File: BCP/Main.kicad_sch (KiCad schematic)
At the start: 7 parts, among them SW1 SW_Nidec_CAS-120A1, U1 LD1117V33, U2 Pico 2, U3 DEV-13712

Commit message: Removed autosave (I swear I know what I'm doing)
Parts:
- added D1, D2, D3, D4: LED, symbol Device:LED
- added Q1: PMOS, symbol Simulation_SPICE:PMOS
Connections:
- net 3.3 V: now also D1.2 (A)
- net GND: now also D2.1 (K), D3.1 (K), D4.1 (K), Q1.1 (D)
- net FLIGHTLED: now reaches U2.24 (GPIO18)
- net FLIGHTLED: now also Q1.2 (G)
- net DEBUG3: now reaches U2.25 (GPIO19)
- net DEBUG3: now also D4.2 (A)
- net DEBUG2: now reaches U2.26 (GPIO20)
- net DEBUG2: now also D3.2 (A)
- net DEBUG1: now reaches U2.27 (GPIO21)
- net DEBUG1: now also D2.2 (A)
- new net: D1.1 (K), Q1.3 (S)
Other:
- note added: "LEDs"
- moved on the sheet: U2

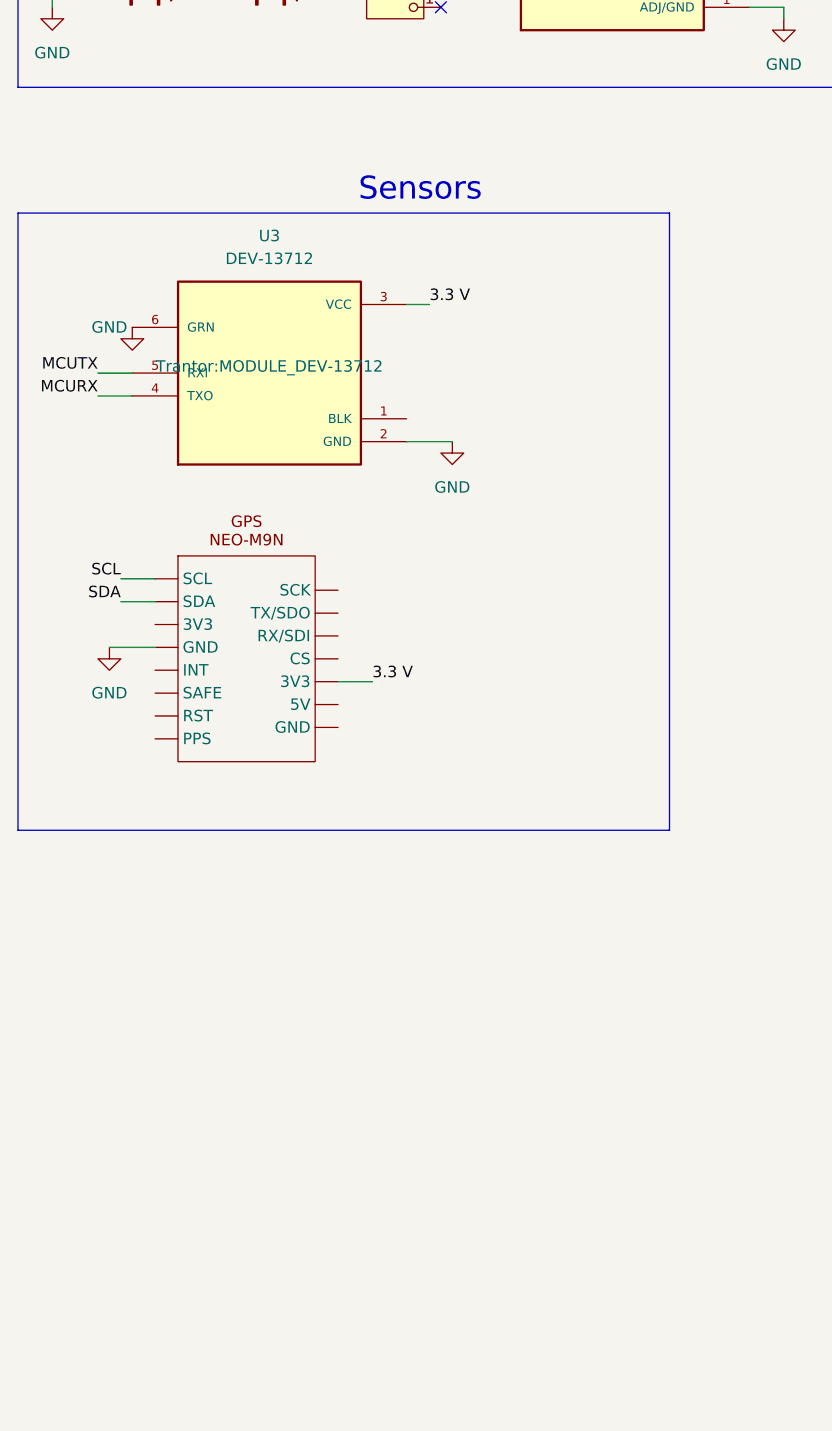
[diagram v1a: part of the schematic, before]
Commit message: Added GPS and BME
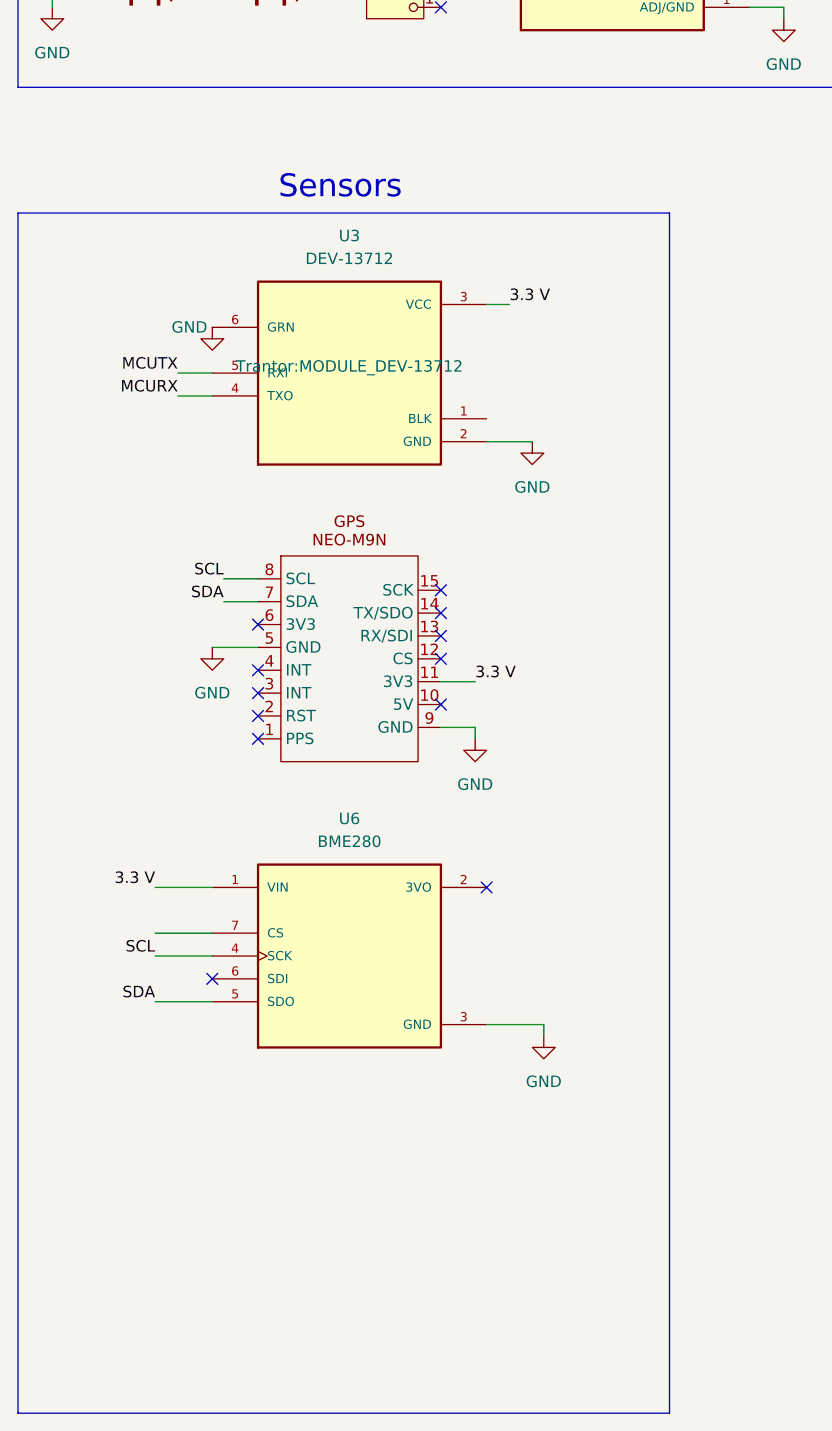
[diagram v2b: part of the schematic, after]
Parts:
- added U6: BME280, Trantor:BME280, symbol Trantor:BME280
- U4: footprint (none) -> Trantor:GPS
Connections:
- net 3.3 V: now also U4.11 (3V3), U6.1 (VIN); no longer U4. (GND)
- net GND: now also U4.5 (GND), U4.9 (GND), U6.3 (GND); no longer U4. (GND)
- net SCL: now also U4.8 (SCL), U6.4 (SCK); no longer U4. (GND)
- net SDA: now also U4.7 (SDA), U6.5 (SDO); no longer U4. (GND)
- no-connect marks 1 -> 13
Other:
- moved on the sheet: U3

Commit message: Theoretically done?
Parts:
- added U5: ~, Trantor:BNO055, symbol Trantor:BNO055
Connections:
- net 3.3 V: now also U5.1 (VIN)
- net GND: now also U5.3 (GND)
- net SCL: now also U5.5 (SCL)
- net SDA: now also U5.4 (SDA)
- no-connect marks 13 -> 19
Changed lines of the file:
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@@
+	)
+	(no_connect
+		(at 46.99 180.34)
 	)
 	(no_connect
@@
 	)
 	(no_connect
+		(at 67.31 177.8)
+	)
+	(no_connect
+		(at 46.99 170.18)
+	)
+	(no_connect
 		(at 45.72 106.68)
 	)
@@
 	)
 	(no_connect
+		(at 67.31 170.18)
+	)
+	(no_connect
 		(at 66.04 110.49)
 	)
@@
 	)
 	(no_connect
+		(at 67.31 175.26)
+	)
+	(no_connect
+		(at 67.31 172.72)
+	)
+	(no_connect
 		(at 66.04 38.1)
 	)
@@
 	(wire
 		(pts
+			(xy 43.18 177.8) (xy 46.99 177.8)
+		)
+		(stroke
+			(width 0)
+			(type default)
+		)
+	)
+	(wire
+		(pts
 			(xy 69.85 118.11) (xy 69.85 119.38)
 		)
@@
 	(wire
 		(pts
+			(xy 36.83 172.72) (xy 46.99 172.72)
+		)
+		(stroke
+			(width 0)
+			(type default)
+		)
+	)
+	(wire
+		(pts
 			(xy 231.14 36.83) (xy 236.22 36.83)
 		)
@@
 	(wire
 		(pts
+			(xy 43.18 175.26) (xy 46.99 175.26)
+		)
+		(stroke
+			(width 0)
+			(type default)
+		)
+	)
+	(wire
+		(pts
 			(xy 250.19 36.83) (xy 246.38 36.83)
 		)
@@
 		(pts
 			(xy 170.18 104.14) (xy 166.37 104.14)
+		)
+		(stroke
+			(width 0)
+			(type default)
+		)
+	)
+	(wire
+		(pts
+			(xy 43.18 167.64) (xy 46.99 167.64)
 		)
 		(stroke
@@
 		)
 	)
+	(label "SCL"
+		(at 43.18 177.8 180)
+		(effects
+			(font
+				(size 1.27 1.27)
+			)
+			(justify right bottom)
+		)
+	)
 	(label "DEBUG1"
 		(at 232.41 57.15 180)
@@
 		)
 	)
+	(label "3.3 V"
+		(at 43.18 167.64 180)
+		(effects
+			(font
+				(size 1.27 1.27)
+			)
+			(justify right bottom)
+		)
+	)
 	(label "SCL"
 		(at 34.29 143.51 180)
@@
 			)
 			(justify left bottom)
+		)
+	)
+	(label "SDA"
+		(at 43.18 175.26 180)
+		(effects
+			(font
+				(size 1.27 1.27)
+			)
+			(justify right bottom)
 		)
 	)
@@
 	)
 	(symbol
+		(lib_id "Trantor:BNO055")
+		(at 57.15 173.99 0)
+		(unit 1)
+		(exclude_from_sim no)
+		(in_bom yes)
+		(on_board yes)
+		(dnp no)
+		(fields_autoplaced yes)
+		(property "Reference" "U5"
+			(at 57.15 160.02 0)
+			(effects
+				(font
+					(size 1.27 1.27)
+				)
+			)
+		)
+		(property "Value" "~"
+			(at 57.15 162.56 0)
+			(effects
+				(font
+					(size 1.27 1.27)
+				)
+			)
+		)
+		(property "Footprint" "Trantor:BNO055"
+			(at 57.15 173.99 0)
+			(effects
+				(font
+					(size 1.27 1.27)
+				)
+				(hide yes)
+			)
+		)
+		(property "Datasheet" ""
+			(at 57.15 173.99 0)
+			(effects
+				(font
+					(size 1.27 1.27)
+				)
+				(hide yes)
+			)
+		)
+		(property "Description" ""
+			(at 57.15 173.99 0)
+			(effects
+				(font
+					(size 1.27 1.27)
+				)
+				(hide yes)
+			)
+		)
+		(pin "4"
+		)
+		(pin "9"
+		)
+		(pin "2"
+		)
+		(pin "1"
+		)
+		(pin "3"
+		)
+		(pin "7"
+		)
+		(pin "5"
+		)
+		(pin "6"
+		)
+		(pin "8"
+		)
+		(pin "10"
+		)
+		(instances
+			(project ""
+				(path "/265d59aa-caac-4c2d-9db5-2e2b992cffbc"
+					(reference "U5")
+					(unit 1)
+				)
+			)
+		)
+	)
+	(symbol
 		(lib_id "power:GND")
 		(at 77.47 152.4 0)
@@
 					(unit 1)
 				)
+			)
+		)
+	)
+	(symbol
+		(lib_id "power:GND")
+		(at 36.83 172.72 0)
+		(unit 1)
+		(exclude_from_sim no)
+		(in_bom yes)
+		(on_board yes)
+		(dnp no)
+		(property "Reference" "#PWR010"
+			(at 36.83 179.07 0)
+			(effects
+				(font
+					(size 1.27 1.27)
+				)
+				(hide yes)
+			)
+		)
+		(property "Value" "GND"
+			(at 33.02 173.228 0)
+			(effects
+				(font
+					(size 1.27 1.27)
+				)
+			)
+		)
+		(property "Footprint" ""
+			(at 36.83 172.72 0)
+			(effects
+				(font
+					(size 1.27 1.27)
+				)
+				(hide yes)
+			)
+		)
+		(property "Datasheet" ""
+			(at 36.83 172.72 0)
+			(effects
+				(font
+					(size 1.27 1.27)
+				)
+				(hide yes)
+			)
+		)
+		(property "Description" "Power symbol creates a global label with name \"GND\" , ground"
+			(at 36.83 172.72 0)
+			(effects
+				(font
+					(size 1.27 1.27)
+				)
+				(hide yes)
+			)
+		)
+		(pin "1"
+		)
+		(instances
+			(project "Main"
+				(path "/265d59aa-caac-4c2d-9db5-2e2b992cffbc"
+					(reference "#PWR010")
+					(unit 1)
+				)
